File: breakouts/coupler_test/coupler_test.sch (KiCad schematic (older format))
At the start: 7 parts, among them U101 CONN_SMA_2GND, U102 resistive_bridge, U103 CONN_SMA_2GND, U104 CONN_SMA_2GND

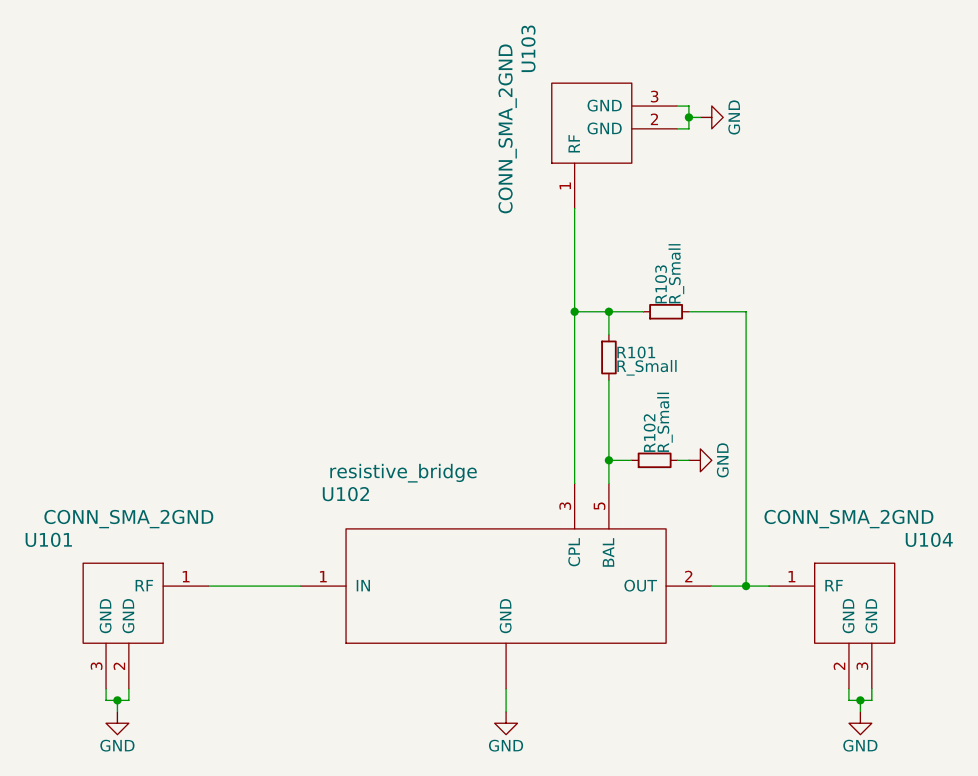
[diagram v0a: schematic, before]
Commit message: cleanup of resistive bridge layout
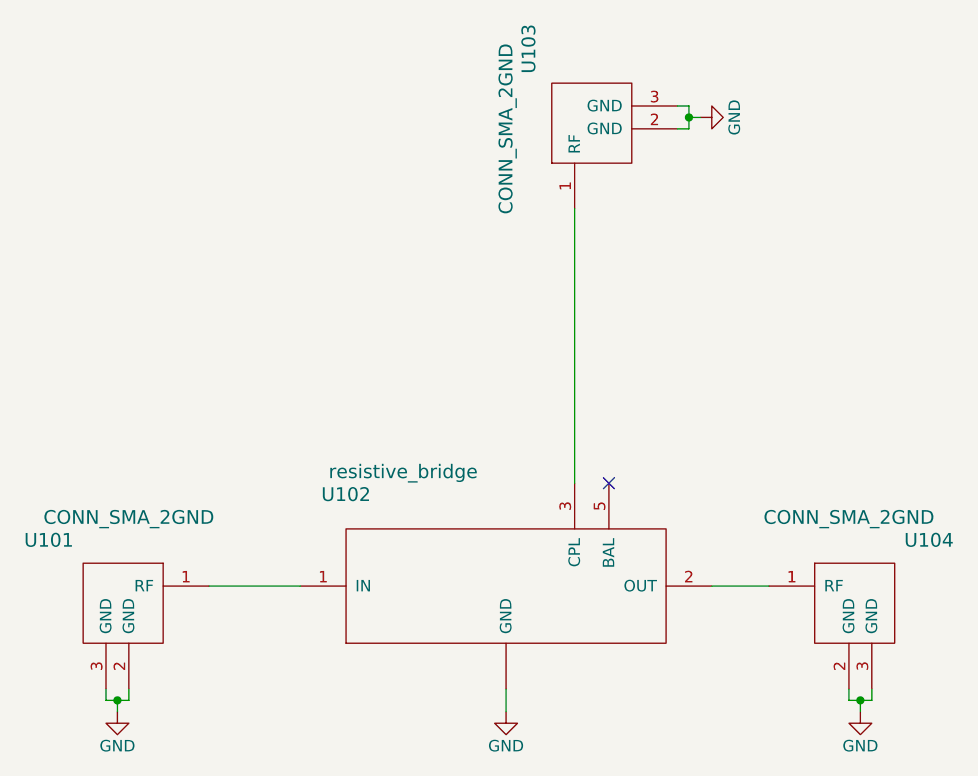
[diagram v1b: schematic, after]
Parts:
- removed R101, R103: R_Small, Resistors_SMD:R_0402, symbol R_Small
- removed R102: R_Small, Resistors_SMD:R_0603, symbol R_Small
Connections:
- no-connect marks 0 -> 1
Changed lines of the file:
@@
 LIBS:resistive_bridge
 LIBS:conn_sma_2gnd
+LIBS:coupler_test-cache
 EELAYER 25 0
 EELAYER END
@@
 	6050 2150 6050 3350
 $Comp
-L R_Small R102
-U 1 1 5A0E2BD4
-P 6400 3250
-F 0 "R102" H 6430 3270 50  0000 L CNN
-F 1 "R_Small" H 6430 3210 50  0000 L CNN
-F 2 "Resistors_SMD:R_0603" H 6400 3250 50  0001 C CNN
-F 3 "" H 6400 3250 50  0001 C CNN
-	1    6400 3250
-	0    -1   -1   0
-$EndComp
-Wire Wire Line
-	6300 3250 6200 3250
-Wire Wire Line
-	6200 2900 6200 3350
-$Comp
-L GND #PWR04
-U 1 1 5A0E2C96
-P 6550 3250
-F 0 "#PWR04" H 6550 3000 50  0001 C CNN
-F 1 "GND" H 6550 3100 50  0000 C CNN
-F 2 "" H 6550 3250 50  0001 C CNN
-F 3 "" H 6550 3250 50  0001 C CNN
-	1    6550 3250
-	0    -1   -1   0
-$EndComp
-Wire Wire Line
-	6550 3250 6500 3250
-$Comp
-L R_Small R101
-U 1 1 5A0E2CF9
-P 6200 2800
-F 0 "R101" H 6230 2820 50  0000 L CNN
-F 1 "R_Small" H 6230 2760 50  0000 L CNN
-F 2 "Resistors_SMD:R_0402" H 6200 2800 50  0001 C CNN
-F 3 "" H 6200 2800 50  0001 C CNN
-	1    6200 2800
-	1    0    0    -1
-$EndComp
-Connection ~ 6200 3250
-Wire Wire Line
-	6050 2600 6350 2600
-Wire Wire Line
-	6200 2600 6200 2700
-Connection ~ 6050 2600
-$Comp
-L R_Small R103
-U 1 1 5A0E2DC5
-P 6450 2600
-F 0 "R103" H 6480 2620 50  0000 L CNN
-F 1 "R_Small" H 6480 2560 50  0000 L CNN
-F 2 "Resistors_SMD:R_0402" H 6450 2600 50  0001 C CNN
-F 3 "" H 6450 2600 50  0001 C CNN
-	1    6450 2600
-	0    -1   -1   0
-$EndComp
-Connection ~ 6200 2600
-Wire Wire Line
-	6550 2600 6800 2600
-Wire Wire Line
-	6800 2600 6800 3800
-Connection ~ 6800 3800
-$Comp
 L GND #PWR?
 U 1 1 5A0E304C
@@
 	6550 1750 6600 1750
 Connection ~ 6550 1750
+NoConn ~ 6200 3350
 $EndSCHEMATC

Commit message: component placement on vna r1 demod
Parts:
- U102: symbol resistive_bridge -> resistive_bridge-RESCUE-coupler_test
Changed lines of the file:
@@
 EESchema Schematic File Version 2
+LIBS:coupler_test-rescue
 LIBS:power
 LIBS:device
@@
 $EndDescr
 $Comp
-L resistive_bridge U102
+L resistive_bridge-RESCUE-coupler_test U102
 U 1 1 5A0E270D
 P 5750 3800
